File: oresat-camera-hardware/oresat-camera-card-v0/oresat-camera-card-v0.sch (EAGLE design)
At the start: 316 parts, among them J1 J-SAMTEC-TFM-120-X1-XXX-D-RA, J2 DM3BT-DSF-PEJS, J4 3-1734592-64-1734592-0, J8 2-1734592-0, Q1 DMP2240UDM, Q3 MIC842, Q4 MIC842, Q5 PMV45EN, Q6 MOSFET-PCH-SOT23-6, Q7 MOSFET-PCH-SOT23-6, Q8 PMV45EN, Q9 MMBT2907, U1 MAX7310ATE, U10 SN74LVC8T245MPWREPPW24-M, U11 RCLAMP0504FB, U12 RCLAMP0504FB, U13 TPS2051CDBVR, U14 TLVH431, U15 SN74LVC1G07DCK, U2 TPS62112, U3 MAX4211CETE, U4 TCAN330, U5 CLVCH16T245MDGGREP, U6 OSD3358-512M-BSM, U7 TCA9509DGKRDGK8-M, U9 TLV70028QDDCRQ1, Y1 24MHz

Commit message: added more labels
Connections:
- net N$25 renamed UART0_TX
- net N$27 renamed UART0_RX
- net N$585: now also R60.77; no longer R60.88
- net N$586: now also R60.44; no longer R60.66
- net N$630: now also R60.99; no longer R60.11
- net N$631: now also R60.11; no longer R60.99
- net N$633: now also R60.88; no longer R60.44
- net N$634: now also R60.33; no longer R60.77
- net N$635: now also R59.88; no longer R59.11
- net N$636: now also R59.33; no longer R59.99
- net N$637: now also R59.22; no longer R59.88
- net N$638: now also R59.99; no longer R59.77
- net N$639: now also R59.11; no longer R59.66
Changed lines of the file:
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@@
 <setting verticaltext="up"/>
 </settings>
-<grid distance="0.1" unitdist="inch" unit="inch" style="lines" multiple="1" display="yes" altdistance="0.05" altunitdist="inch" altunit="inch"/>
+<grid distance="0.1" unitdist="inch" unit="inch" style="lines" multiple="1" display="no" altdistance="0.01" altunitdist="inch" altunit="inch"/>
 <layers>
 <layer number="1" name="Top" color="4" fill="1" visible="no" active="no"/>
@@
 <segment>
 <pinref part="U6" gate="D" pin="LCD_DATA5"/>
-<wire x1="635" y1="375.92" x2="690.88" y2="375.92" width="0.1524" layer="91"/>
-<wire x1="690.88" y1="375.92" x2="690.88" y2="345.44" width="0.1524" layer="91"/>
-<pinref part="R60" gate="A" pin="88"/>
+<wire x1="635" y1="375.92" x2="685.8" y2="375.92" width="0.1524" layer="91"/>
+<wire x1="685.8" y1="375.92" x2="685.8" y2="345.44" width="0.1524" layer="91"/>
+<pinref part="R60" gate="A" pin="77"/>
 </segment>
 </net>
@@
 <segment>
 <pinref part="U6" gate="D" pin="LCD_DATA6"/>
-<wire x1="635" y1="373.38" x2="680.72" y2="373.38" width="0.1524" layer="91"/>
-<wire x1="680.72" y1="373.38" x2="680.72" y2="345.44" width="0.1524" layer="91"/>
-<pinref part="R60" gate="A" pin="66"/>
+<wire x1="635" y1="373.38" x2="683.26" y2="373.38" width="0.1524" layer="91"/>
+<wire x1="683.26" y1="373.38" x2="683.26" y2="345.44" width="0.1524" layer="91"/>
+<pinref part="R60" gate="A" pin="44"/>
 </segment>
 </net>
@@
 <segment>
 <pinref part="J7" gate="G$1" pin="1"/>
-<wire x1="698.5" y1="345.44" x2="698.5" y2="363.22" width="0.1524" layer="91"/>
-<wire x1="698.5" y1="363.22" x2="703.58" y2="363.22" width="0.1524" layer="91"/>
-<pinref part="R60" gate="A" pin="11"/>
+<wire x1="695.96" y1="345.44" x2="695.96" y2="363.22" width="0.1524" layer="91"/>
+<wire x1="695.96" y1="363.22" x2="703.58" y2="363.22" width="0.1524" layer="91"/>
+<pinref part="R60" gate="A" pin="99"/>
 </segment>
 </net>
@@
 <segment>
 <pinref part="J7" gate="G$1" pin="2"/>
-<wire x1="695.96" y1="345.44" x2="695.96" y2="360.68" width="0.1524" layer="91"/>
-<wire x1="695.96" y1="360.68" x2="703.58" y2="360.68" width="0.1524" layer="91"/>
-<pinref part="R60" gate="A" pin="99"/>
+<wire x1="698.5" y1="345.44" x2="698.5" y2="360.68" width="0.1524" layer="91"/>
+<wire x1="698.5" y1="360.68" x2="703.58" y2="360.68" width="0.1524" layer="91"/>
+<pinref part="R60" gate="A" pin="11"/>
 </segment>
 </net>
@@
 <segment>
 <pinref part="J7" gate="G$1" pin="4"/>
-<wire x1="683.26" y1="345.44" x2="683.26" y2="355.6" width="0.1524" layer="91"/>
-<wire x1="683.26" y1="355.6" x2="703.58" y2="355.6" width="0.1524" layer="91"/>
-<pinref part="R60" gate="A" pin="44"/>
+<wire x1="690.88" y1="345.44" x2="690.88" y2="355.6" width="0.1524" layer="91"/>
+<wire x1="690.88" y1="355.6" x2="703.58" y2="355.6" width="0.1524" layer="91"/>
+<pinref part="R60" gate="A" pin="88"/>
 </segment>
 </net>
@@
 <segment>
 <pinref part="J7" gate="G$1" pin="5"/>
-<wire x1="703.58" y1="353.06" x2="685.8" y2="353.06" width="0.1524" layer="91"/>
-<wire x1="685.8" y1="353.06" x2="685.8" y2="345.44" width="0.1524" layer="91"/>
-<pinref part="R60" gate="A" pin="77"/>
+<wire x1="703.58" y1="353.06" x2="688.34" y2="353.06" width="0.1524" layer="91"/>
+<wire x1="688.34" y1="353.06" x2="688.34" y2="345.44" width="0.1524" layer="91"/>
+<pinref part="R60" gate="A" pin="33"/>
 </segment>
 </net>
@@
 <segment>
 <pinref part="J5" gate="G$1" pin="1"/>
-<wire x1="703.58" y1="414.02" x2="680.72" y2="414.02" width="0.1524" layer="91"/>
-<wire x1="680.72" y1="414.02" x2="680.72" y2="419.1" width="0.1524" layer="91"/>
-<pinref part="R59" gate="A" pin="11"/>
+<wire x1="703.58" y1="414.02" x2="688.34" y2="414.02" width="0.1524" layer="91"/>
+<wire x1="688.34" y1="414.02" x2="688.34" y2="419.1" width="0.1524" layer="91"/>
+<pinref part="R59" gate="A" pin="88"/>
 </segment>
 </net>
@@
 <segment>
 <pinref part="J5" gate="G$1" pin="2"/>
-<wire x1="703.58" y1="411.48" x2="683.26" y2="411.48" width="0.1524" layer="91"/>
-<wire x1="683.26" y1="411.48" x2="683.26" y2="419.1" width="0.1524" layer="91"/>
-<pinref part="R59" gate="A" pin="99"/>
+<wire x1="703.58" y1="411.48" x2="690.88" y2="411.48" width="0.1524" layer="91"/>
+<wire x1="690.88" y1="411.48" x2="690.88" y2="419.1" width="0.1524" layer="91"/>
+<pinref part="R59" gate="A" pin="33"/>
 </segment>
 </net>
@@
 <segment>
 <pinref part="J5" gate="G$1" pin="3"/>
-<wire x1="703.58" y1="408.94" x2="688.34" y2="408.94" width="0.1524" layer="91"/>
-<wire x1="688.34" y1="408.94" x2="688.34" y2="419.1" width="0.1524" layer="91"/>
-<pinref part="R59" gate="A" pin="88"/>
+<wire x1="703.58" y1="408.94" x2="685.8" y2="408.94" width="0.1524" layer="91"/>
+<wire x1="685.8" y1="408.94" x2="685.8" y2="419.1" width="0.1524" layer="91"/>
+<pinref part="R59" gate="A" pin="22"/>
 </segment>
 </net>
@@
 <segment>
 <pinref part="J5" gate="G$1" pin="4"/>
-<wire x1="703.58" y1="406.4" x2="693.42" y2="406.4" width="0.1524" layer="91"/>
-<wire x1="693.42" y1="406.4" x2="693.42" y2="419.1" width="0.1524" layer="91"/>
-<pinref part="R59" gate="A" pin="77"/>
+<wire x1="703.58" y1="406.4" x2="683.26" y2="406.4" width="0.1524" layer="91"/>
+<wire x1="683.26" y1="406.4" x2="683.26" y2="419.1" width="0.1524" layer="91"/>
+<pinref part="R59" gate="A" pin="99"/>
 </segment>
 </net>
@@
 <segment>
 <pinref part="J5" gate="G$1" pin="5"/>
-<wire x1="703.58" y1="403.86" x2="698.5" y2="403.86" width="0.1524" layer="91"/>
-<wire x1="698.5" y1="403.86" x2="698.5" y2="419.1" width="0.1524" layer="91"/>
-<pinref part="R59" gate="A" pin="66"/>
+<wire x1="703.58" y1="403.86" x2="680.72" y2="403.86" width="0.1524" layer="91"/>
+<wire x1="680.72" y1="403.86" x2="680.72" y2="419.1" width="0.1524" layer="91"/>
+<pinref part="R59" gate="A" pin="11"/>
 </segment>
 </net>
@@
 </segment>
 </net>
-<net name="N$25" class="0">
+<net name="UART0_TX" class="0">
 <segment>
 <pinref part="U6" gate="C" pin="UART0_TXD"/>
-<wire x1="289.56" y1="406.4" x2="289.56" y2="419.1" width="0.1524" layer="91"/>
-<wire x1="289.56" y1="419.1" x2="294.64" y2="419.1" width="0.1524" layer="91"/>
+<wire x1="289.56" y1="406.4" x2="289.56" y2="414.02" width="0.1524" layer="91"/>
+<wire x1="289.56" y1="414.02" x2="294.64" y2="414.02" width="0.1524" layer="91"/>
 <pinref part="J3" gate="J$1" pin="2"/>
-<wire x1="294.64" y1="419.1" x2="294.64" y2="444.5" width="0.1524" layer="91"/>
+<wire x1="294.64" y1="414.02" x2="294.64" y2="444.5" width="0.1524" layer="91"/>
+<label x="294.64" y="419.1" size="1.778" layer="95" rot="R90"/>
 </segment>
 </net>
-<net name="N$27" class="0">
+<net name="UART0_RX" class="0">
 <segment>
 <pinref part="J3" gate="J$1" pin="1"/>
-<wire x1="292.1" y1="444.5" x2="292.1" y2="421.64" width="0.1524" layer="91"/>
-<wire x1="292.1" y1="421.64" x2="287.02" y2="421.64" width="0.1524" layer="91"/>
+<wire x1="292.1" y1="444.5" x2="292.1" y2="416.56" width="0.1524" layer="91"/>
+<wire x1="292.1" y1="416.56" x2="287.02" y2="416.56" width="0.1524" layer="91"/>
 <pinref part="U6" gate="C" pin="UART0_RXD"/>
-<wire x1="287.02" y1="421.64" x2="287.02" y2="403.86" width="0.1524" layer="91"/>
+<wire x1="287.02" y1="416.56" x2="287.02" y2="403.86" width="0.1524" layer="91"/>
 <wire x1="287.02" y1="403.86" x2="289.56" y2="403.86" width="0.1524" layer="91"/>
+<label x="292.1" y="419.1" size="1.778" layer="95" rot="R90"/>
 </segment>
 </net>

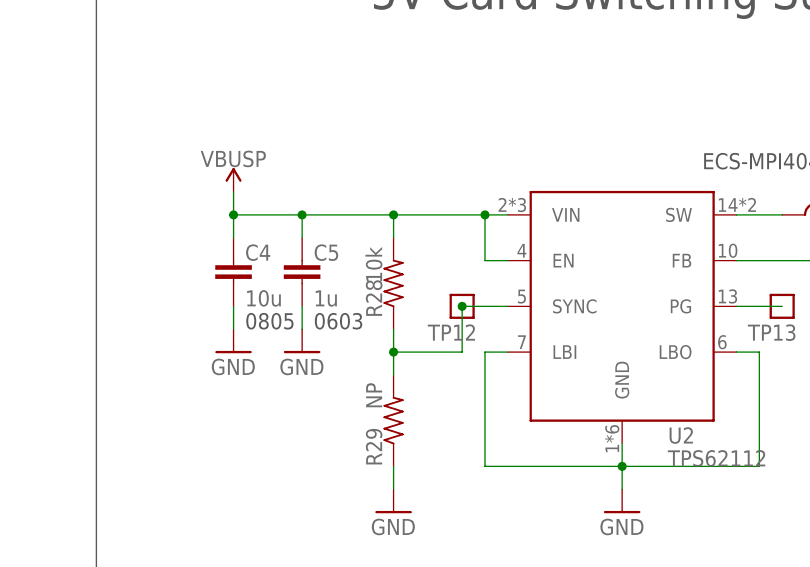
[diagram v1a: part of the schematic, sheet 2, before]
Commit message: added silk on resistors
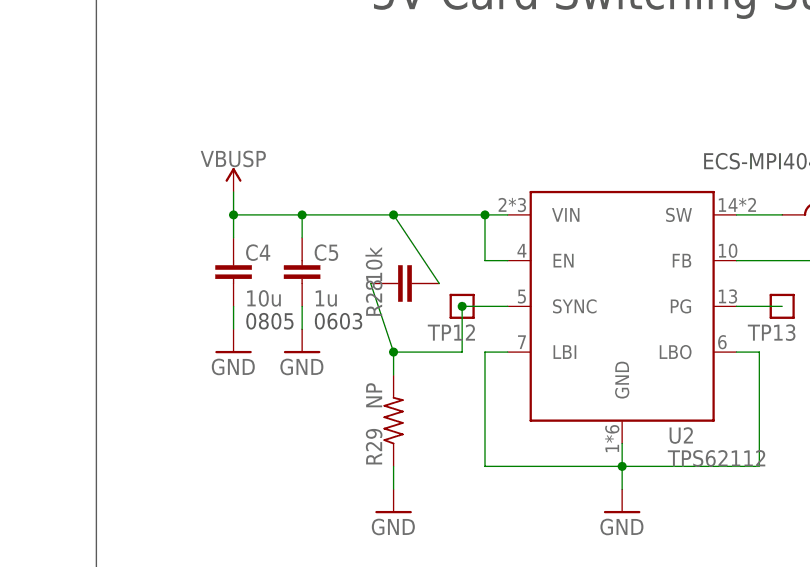
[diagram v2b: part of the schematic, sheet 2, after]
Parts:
- C10, C11, C12, C13, C14, C15, C16, C17, C18, C19, C20, C21, C22, C23, C24, C25, C26, C27, C28, C29, C3, C30, C32, C35, C36, C39, C5, C6, C7, C9: device oresat-rcl:C-EU0603-A-NOSILK -> oresat-rcl:C-EU0603-A
- R1, R10, R11, R12, R13, R14, R15, R16, R17, R18, R19, R2, R20, R21, R22, R23, R24, R25, R26, R27, R29, R3, R30, R31, R33, R34, R35, R36, R37, R38, R39, R4, R40, R41, R43, R44, R45, R46, R47, R5, R54, R55, R56, R57, R6, R63, R64, R65, R66, R7, R8, R9: device oresat-rcl:R-US_0603-A-NOSILK -> oresat-rcl:R-US_0603-A
- R28: device oresat-rcl:R-US_0603-A-NOSILK -> oresat-rcl:C-EU0603-A

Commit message: moved chip a bit
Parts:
- C31, C33, C34: device oresat-rcl:C-EU0603-A-NOSILK -> oresat-rcl:C-EU0603-A
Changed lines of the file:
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@@
 <part name="Y1" library="X-ECS-240-12-30BQ-AEN-TR" deviceset="ECS-240-12-30BQ-AEN-TR" device="" value="24MHz"/>
 <part name="GND56" library="SparkFun-PowerSymbols" deviceset="GND" device=""/>
-<part name="C34" library="oresat-rcl" deviceset="C-EU" device="0603-A-NOSILK" value="0.1uF"/>
-<part name="C31" library="oresat-rcl" deviceset="C-EU" device="0603-A-NOSILK" value="1nF"/>
-<part name="C33" library="oresat-rcl" deviceset="C-EU" device="0603-A-NOSILK" value="0.1uF"/>
+<part name="C34" library="oresat-rcl" deviceset="C-EU" device="0603-A" value="0.1uF"/>
+<part name="C31" library="oresat-rcl" deviceset="C-EU" device="0603-A" value="1nF"/>
+<part name="C33" library="oresat-rcl" deviceset="C-EU" device="0603-A" value="0.1uF"/>
 <part name="R63" library="oresat-rcl" deviceset="R-US_" device="0603-A" value="0"/>
 <part name="AGND1" library="SparkFun-PowerSymbols" deviceset="AGND" device=""/>

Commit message: last minute changes
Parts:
- added TP151: TEST-POINT3X4, SparkFun-Connectors:TEST-POINT3X4
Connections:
- net N$3: now also TP151.1
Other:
- note added: "TODO add optional resistors from AM335X datasheet?"
- note removed: "Power Button TODO Label in silk TODO does OPD need this?"
- note removed: "TODO GND test points"
- note removed: "TODO add optional resistors from AM335X datasheet"
- note removed: "TODO this connector has a crappy footprint get a new one"
- moved on the sheet: TP112
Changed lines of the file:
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@@
 <part name="TP149" library="SparkFun-Connectors" deviceset="TEST-POINT" device="3X4"/>
 <part name="TP150" library="Tova" deviceset="TEST-POINT" device=""/>
+<part name="TP151" library="SparkFun-Connectors" deviceset="TEST-POINT" device="3X4"/>
 </parts>
 <sheets>
@@
 <description>OSD3358 SD, eMMC, Camera, etc : SIP C, D</description>
 <plain>
-<text x="111.76" y="523.24" size="1.778" layer="97">TODO
-GND test points
-</text>
 <text x="718.82" y="383.54" size="1.778" layer="97">SYSBOOT Jumper to config boot order
 must use very light pullups because
@@
 <text x="71.12" y="177.8" size="2.54" layer="97">JTAG connector</text>
 <text x="99.06" y="104.14" size="2.54" layer="97">USB Client Circuit</text>
-<text x="106.68" y="48.26" size="1.778" layer="101">TODO this connector has a crappy footprint
-get a new one</text>
 <text x="293.624" y="197.358" size="1.778" layer="97">Analog section taken straight from RED board
 schematic, something about ADC monitoring
@@
 <text x="101.6" y="66.04" size="1.778" layer="97">See Connectors Sheet</text>
 <text x="322.58" y="71.12" size="1.778" layer="97">See Connectors Sheet</text>
-<text x="81.28" y="251.46" size="1.778" layer="97">TODO add optional resistors from AM335X datasheet</text>
+<text x="99.06" y="254" size="1.778" layer="97">TODO add optional resistors from AM335X datasheet?</text>
 <text x="154.94" y="243.84" size="1.778" layer="97">XTALIN</text>
 <text x="154.94" y="228.6" size="1.778" layer="97">XTALOUT</text>
@@
 <attribute name="VALUE" x="286.385" y="188.595" size="1.27" layer="96"/>
 </instance>
-<instance part="TP112" gate="G$1" x="254" y="167.64" smashed="yes" rot="R90">
-<attribute name="NAME" x="254.762" y="172.212" size="1.778" layer="95" font="vector" rot="R90"/>
+<instance part="TP112" gate="G$1" x="264.16" y="167.64" smashed="yes" rot="R90">
+<attribute name="NAME" x="264.922" y="172.212" size="1.778" layer="95" font="vector" rot="R90"/>
 </instance>
 <instance part="TP101" gate="G$1" x="167.64" y="193.04" smashed="yes" rot="R180">
@@
 <attribute name="NAME" x="297.18" y="145.161" size="1.778" layer="95" font="vector"/>
 </instance>
+<instance part="TP151" gate="G$1" x="243.84" y="177.8" smashed="yes">
+<attribute name="NAME" x="248.412" y="177.038" size="1.778" layer="95" font="vector"/>
+</instance>
 </instances>
 <busses>
@@
 <net name="PMIC_MUX_IN" class="0">
 <segment>
-<wire x1="231.14" y1="167.64" x2="254" y2="167.64" width="0.1524" layer="91"/>
+<wire x1="231.14" y1="167.64" x2="264.16" y2="167.64" width="0.1524" layer="91"/>
 <pinref part="R66" gate="R" pin="2"/>
-<wire x1="254" y1="167.64" x2="287.02" y2="167.64" width="0.1524" layer="91"/>
+<wire x1="264.16" y1="167.64" x2="287.02" y2="167.64" width="0.1524" layer="91"/>
 <wire x1="287.02" y1="165.1" x2="287.02" y2="167.64" width="0.1524" layer="91"/>
 <pinref part="R65" gate="R" pin="1"/>
@@
 <pinref part="U6" gate="B" pin="PMIC_MUX_IN"/>
 <pinref part="TP112" gate="G$1" pin="1"/>
-<junction x="254" y="167.64"/>
+<junction x="264.16" y="167.64"/>
 </segment>
 </net>
@@
 <wire x1="243.84" y1="172.72" x2="243.84" y2="177.8" width="0.1524" layer="91"/>
 <wire x1="243.84" y1="177.8" x2="231.14" y2="177.8" width="0.1524" layer="91"/>
+<pinref part="TP151" gate="G$1" pin="1"/>
+<junction x="243.84" y="177.8"/>
 </segment>
 </net>
@@
 ready. Because of different voltage levels,
 an open-drain buffer is required.</text>
-<text x="-203.2" y="157.48" size="1.778" layer="97">PWR from USB client circuit</text>
+<text x="-208.28" y="157.48" size="1.778" layer="97">PWR from USB client circuit</text>
 <text x="-182.88" y="193.04" size="1.778" layer="97">Jumper to disconnect
 octavo from OPD power</text>
@@
 <wire x1="17.78" y1="182.88" x2="17.78" y2="210.82" width="0.1524" layer="97"/>
 <wire x1="17.78" y1="210.82" x2="-38.1" y2="210.82" width="0.1524" layer="97"/>
-<wire x1="-170.18" y1="162.56" x2="-205.74" y2="162.56" width="0.1524" layer="97"/>
-<wire x1="-205.74" y1="162.56" x2="-205.74" y2="154.94" width="0.1524" layer="97"/>
-<wire x1="-205.74" y1="154.94" x2="-170.18" y2="154.94" width="0.1524" layer="97"/>
-<wire x1="-170.18" y1="154.94" x2="-170.18" y2="162.56" width="0.1524" layer="97"/>
+<wire x1="-175.26" y1="162.56" x2="-210.82" y2="162.56" width="0.1524" layer="97"/>
+<wire x1="-210.82" y1="162.56" x2="-210.82" y2="154.94" width="0.1524" layer="97"/>
+<wire x1="-210.82" y1="154.94" x2="-175.26" y2="154.94" width="0.1524" layer="97"/>
+<wire x1="-175.26" y1="154.94" x2="-175.26" y2="162.56" width="0.1524" layer="97"/>
 <text x="-175.26" y="-7.62" size="1.778" layer="150">RTC_KALDO_ENN is grounded thru a 10K ohm resistor so that
 the internal RTC LDO is enabled and CAP_VDD_RTC does not
@@
 <wire x1="-154.94" y1="190.5" x2="-154.94" y2="200.66" width="0.1524" layer="97"/>
 <wire x1="-154.94" y1="200.66" x2="-185.42" y2="200.66" width="0.1524" layer="97"/>
-<text x="-194.564" y="94.996" size="1.778" layer="97">Power Button
-TODO Label in silk
-TODO does OPD need this?</text>
+<text x="-194.564" y="94.996" size="1.778" layer="97"></text>
 </plain>
 <instances>
